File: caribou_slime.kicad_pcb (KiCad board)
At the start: 2 copper layers, 62.7 x 37.6 mm, 37 parts, among them J1 BATT JST, Q1 AO3145, U1 ESP32-C3_SUPERMINI, U2 BMI270, U3 FS312F-G, U4 FS8205A, U5 TP4056, U6 ME6211C33M5G

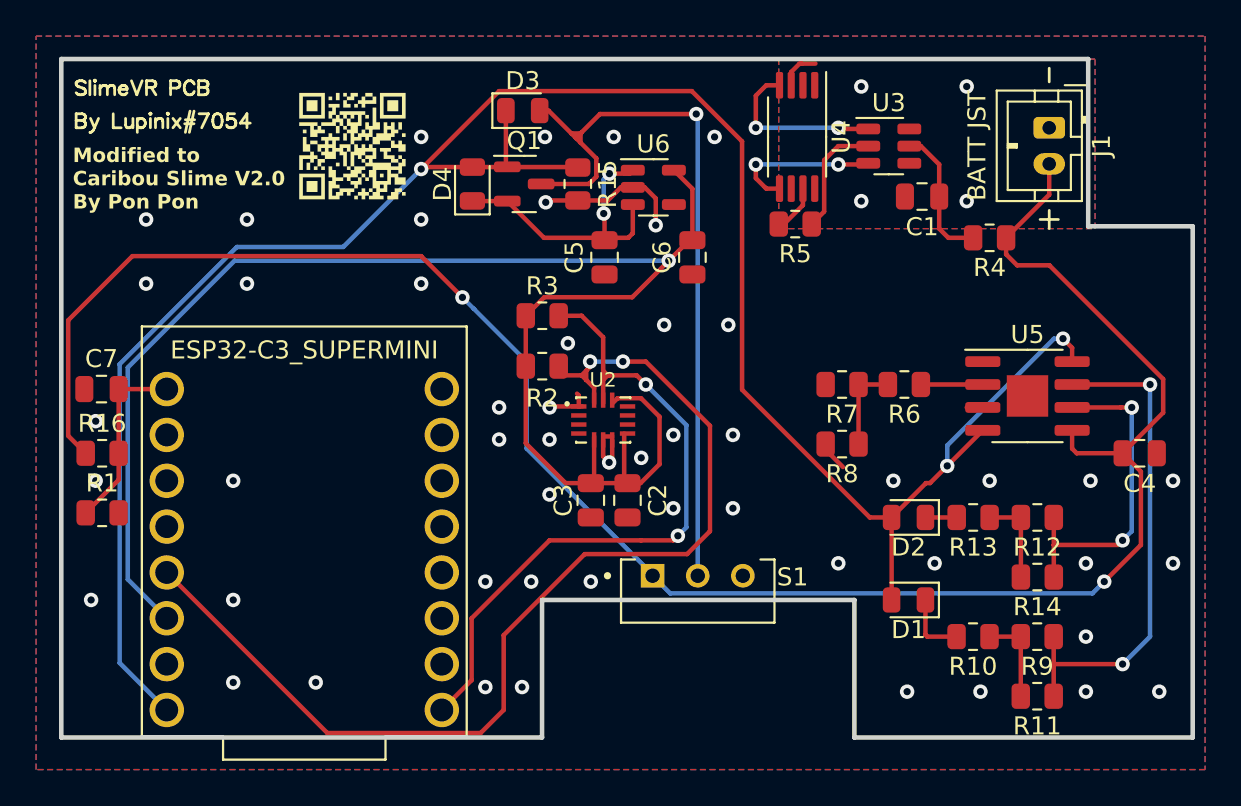
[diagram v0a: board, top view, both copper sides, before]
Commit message: chore(pcb): Improve regulator aesthetics
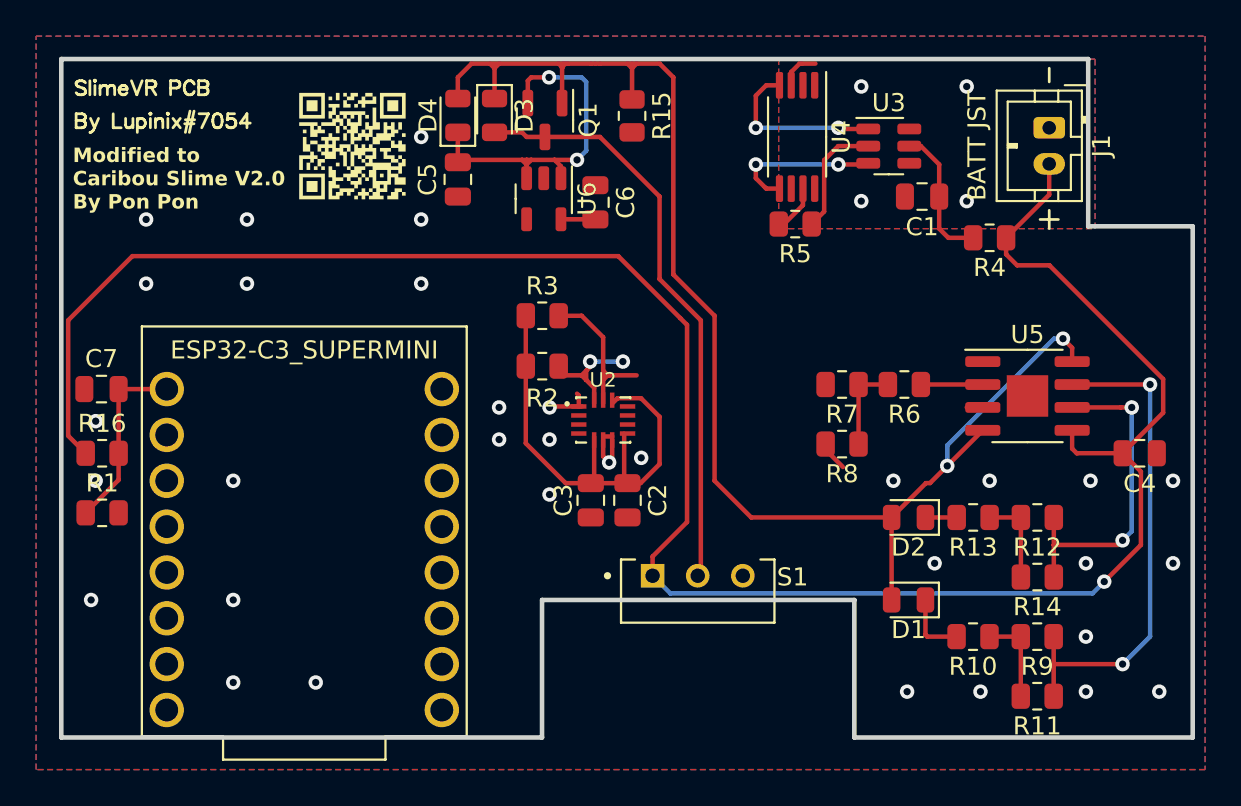
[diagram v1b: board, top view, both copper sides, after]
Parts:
- moved C5 9.20 mm to (47.5, 32.1)
- moved C6 6.18 mm to (55.1, 33.3), turned to -90 degrees
- moved U6 6.10 mm to (52.3, 33.1), turned to -90 degrees
- moved R15 4.82 mm to (57.1, 28.6)
- moved D4 3.88 mm to (47.5, 28.5)
- moved Q1 3.73 mm to (52.3, 28.8), turned to -90 degrees
- moved D3 1.59 mm to (49.5, 28.5), turned to -90 degrees
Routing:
- net +3V3: track 89.6 -> 29.0 mm, vias 1 -> 0
- net SDA: track 59.4 -> 6.40 mm
- net +5V: track 122.1 -> 78.8 mm, vias 3 -> 2
- net SCL: track 38.6 -> 9.28 mm, vias 2 -> 0
- net Net-(D3-A): track 42.4 -> 32.6 mm, vias 1 -> 0
- net GND: track 19.2 -> 11.0 mm, vias 51 -> 33
- net VBAT: track 112.4 -> 120.5 mm, vias 2 -> 1
- net Net-(D4-K): track 16.6 -> 20.4 mm

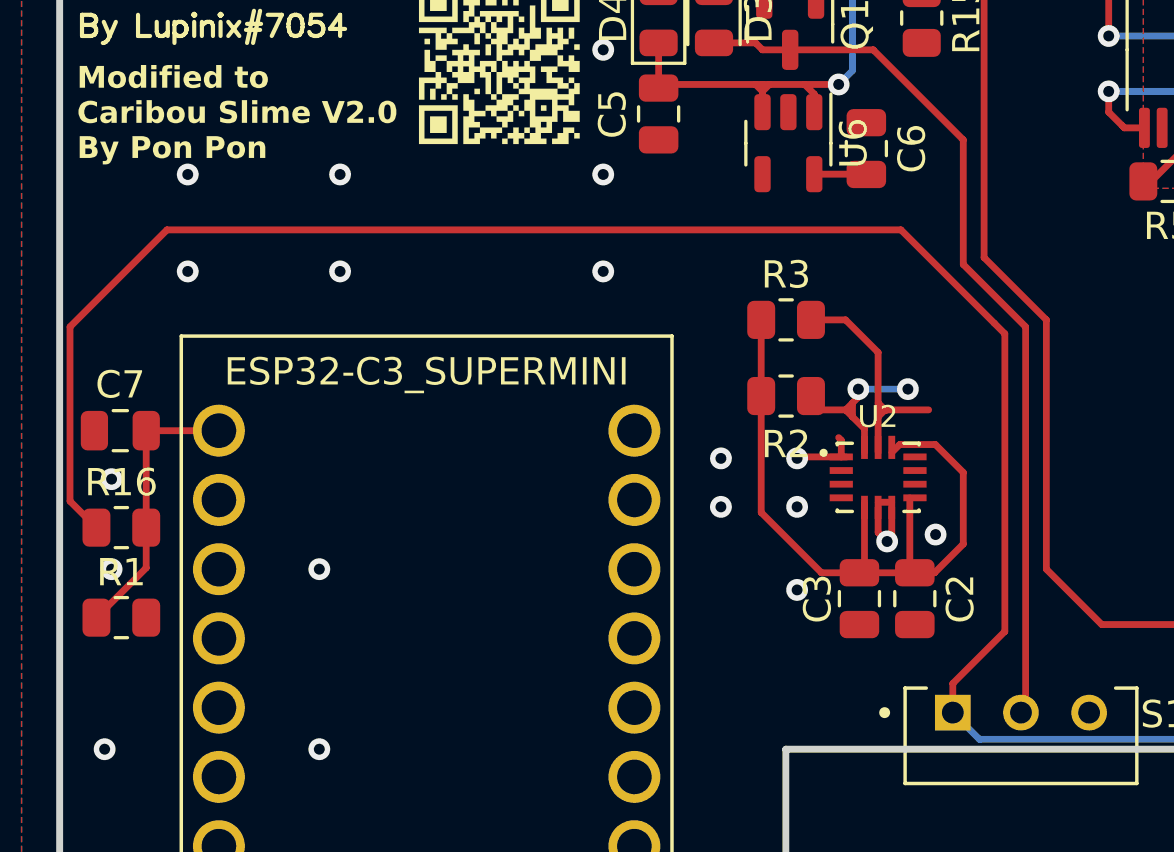
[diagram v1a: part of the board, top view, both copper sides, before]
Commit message: chore(pcb): Improve BMI270 aesthetics
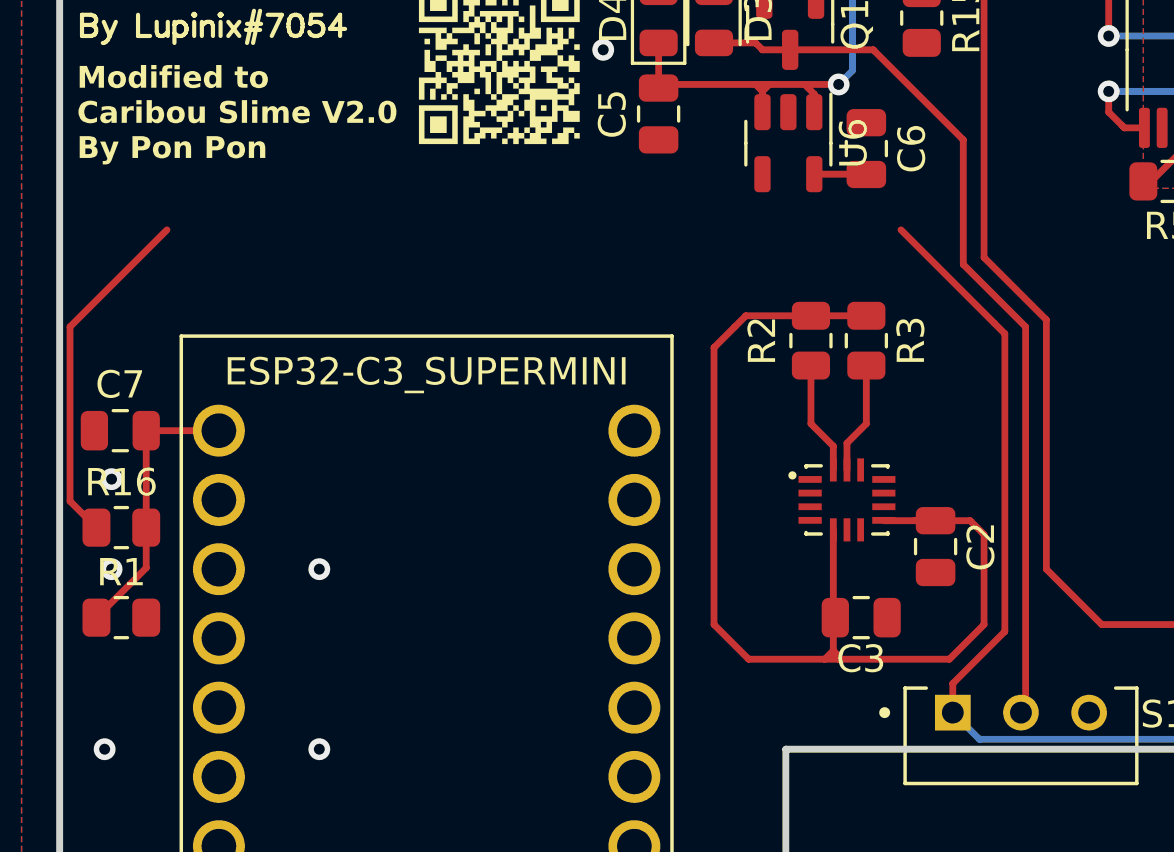
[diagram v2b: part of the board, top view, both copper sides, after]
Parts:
- moved R3 3.04 mm to (55.1, 40.4), turned to -90 degrees
- moved R2 2.23 mm to (53.1, 40.4), turned to -90 degrees
- moved C2 2.06 mm to (57.7, 47.9)
- moved U2 1.41 mm to (54.4, 46.2)
- moved C3 0.70 mm to (54.9, 50.5), turned to 0 degrees
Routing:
- net VBAT: track 120.5 -> 93.5 mm
- net +3V3: track 29.0 -> 41.6 mm
- net GND: track 11.0 -> 5.25 mm, vias 33 -> 20
- net SCL: track 9.28 -> 4.12 mm
- net SDA: track 6.40 -> 4.17 mm, vias 2 -> 0

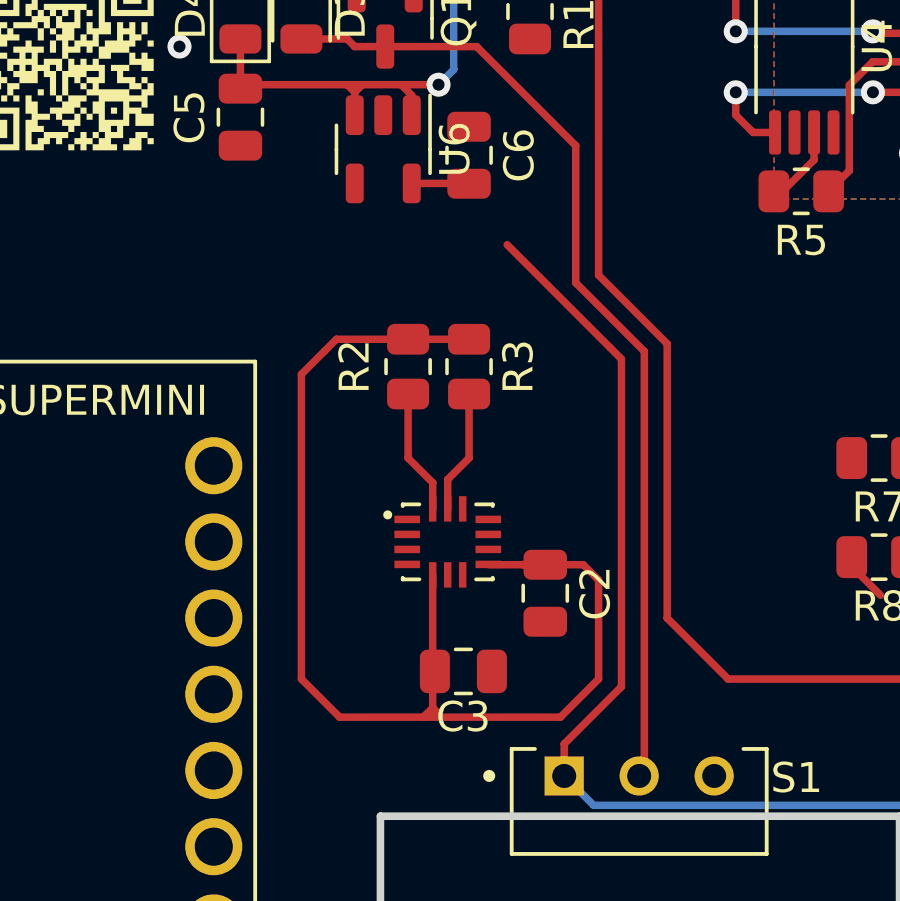
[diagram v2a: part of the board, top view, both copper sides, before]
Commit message: chore(pcb): Improve 270/regulator aesthetics
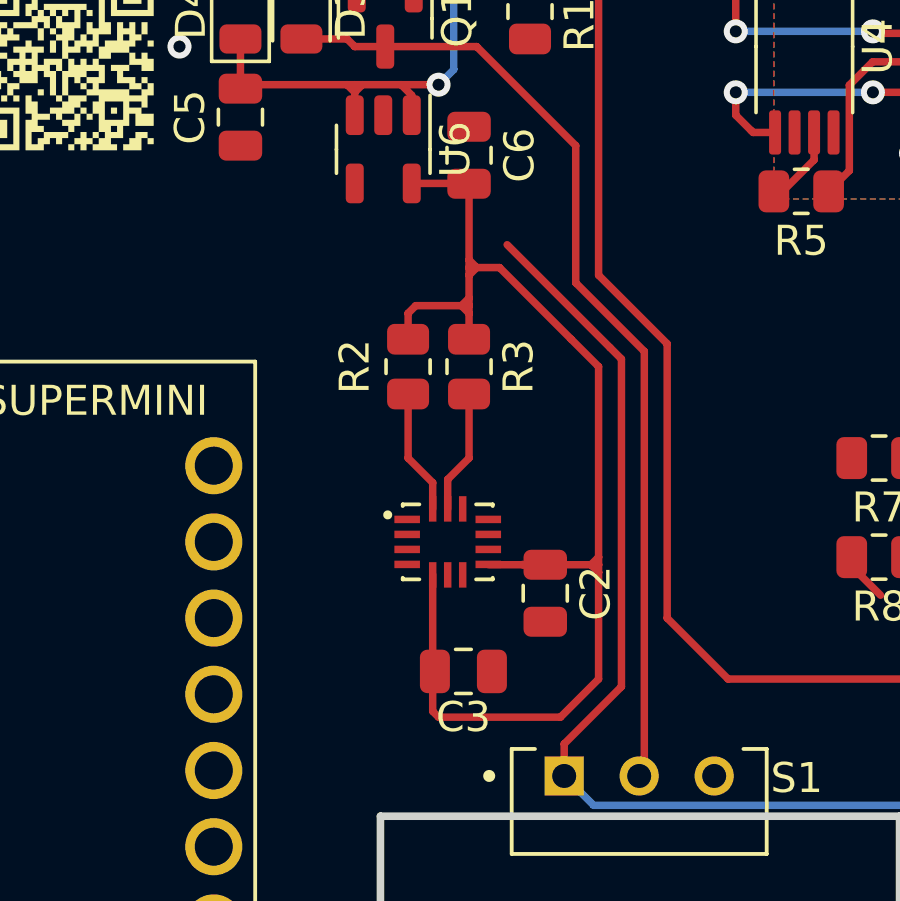
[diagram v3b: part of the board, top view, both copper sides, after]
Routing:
- net +3V3: track 41.6 -> 42.7 mm
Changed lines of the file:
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@@
     (style (thickness 0.15) (arrow_length 1.27) (text_position_mode 0) (extension_height 0.58642) (extension_offset 0.5) keep_text_aligned)
   )
+  (segment (start 59.436 47.244) (end 59.436 46.99) (width 0.25) (layer "F.Cu") (net 1))
+  (segment (start 55.118 34.29) (end 55.118 36.83) (width 0.25) (layer "F.Cu") (net 1))
   (segment (start 55.107 34.279) (end 55.118 34.29) (width 0.25) (layer "F.Cu") (net 1))
-  (segment (start 54.102 52.07) (end 53.594 52.07) (width 0.25) (layer "F.Cu") (net 1))
-  (segment (start 57.658 46.99) (end 58.928 46.99) (width 0.25) (layer "F.Cu") (net 1))
+  (segment (start 55.372 37.084) (end 55.118 37.084) (width 0.25) (layer "F.Cu") (net 1))
+  (segment (start 55.118 38.1) (end 55.118 38.354) (width 0.25) (layer "F.Cu") (net 1))
+  (segment (start 53.34 38.354) (end 54.864 38.354) (width 0.25) (layer "F.Cu") (net 1))
+  (segment (start 59.436 46.736) (end 59.436 40.386) (width 0.25) (layer "F.Cu") (net 1))
+  (segment (start 59.182 46.99) (end 59.436 46.99) (width 0.25) (layer "F.Cu") (net 1))
+  (segment (start 55.118 38.354) (end 55.118 38.608) (width 0.25) (layer "F.Cu") (net 1))
+  (segment (start 58.5235 39.4735) (end 56.134 37.084) (width 0.25) (layer "F.Cu") (net 1))
+  (segment (start 54.102 52.07) (end 58.166 52.07) (width 0.25) (layer "F.Cu") (net 1))
+  (segment (start 59.436 46.99) (end 59.436 46.736) (width 0.25) (layer "F.Cu") (net 1))
+  (segment (start 54.864 38.354) (end 55.118 38.354) (width 0.25) (layer "F.Cu") (net 1))
+  (segment (start 59.436 50.8) (end 59.436 47.244) (width 0.25) (layer "F.Cu") (net 1))
+  (segment (start 58.166 52.07) (end 59.436 50.8) (width 0.25) (layer "F.Cu") (net 1))
   (segment (start 53.208 34.279) (end 55.107 34.279) (width 0.25) (layer "F.Cu") (net 1))
-  (segment (start 53.594 52.07) (end 50.8 52.07) (width 0.25) (layer "F.Cu") (net 1))
   (segment (start 57.658 46.99) (end 55.7705 46.99) (width 0.25) (layer "F.Cu") (net 1))
-  (segment (start 59.436 50.8) (end 58.166 52.07) (width 0.25) (layer "F.Cu") (net 1))
-  (segment (start 53.907 51.757) (end 53.594 52.07) (width 0.25) (layer "F.Cu") (net 1))
+  (segment (start 55.118 37.084) (end 55.118 37.338) (width 0.25) (layer "F.Cu") (net 1))
+  (segment (start 59.182 46.99) (end 59.436 46.736) (width 0.25) (layer "F.Cu") (net 1))
+  (segment (start 53.907 51.875) (end 54.102 52.07) (width 0.25) (layer "F.Cu") (net 1))
+  (segment (start 53.086 38.608) (end 53.34 38.354) (width 0.25) (layer "F.Cu") (net 1))
   (segment (start 56.9135 46.99) (end 56.9015 46.978) (width 0.25) (layer "F.Cu") (net 1))
-  (segment (start 49.53 50.8) (end 50.8 52.07) (width 0.25) (layer "F.Cu") (net 1))
-  (segment (start 53.907 51.757) (end 54.102 51.952) (width 0.25) (layer "F.Cu") (net 1))
-  (segment (start 53.907 47.3275) (end 53.907 51.757) (width 0.25) (layer "F.Cu") (net 1))
-  (segment (start 49.53 40.64) (end 50.292 39.878) (width 0.25) (layer "F.Cu") (net 1))
-  (segment (start 58.928 46.99) (end 59.436 47.498) (width 0.25) (layer "F.Cu") (net 1))
-  (segment (start 54.102 51.952) (end 54.102 52.07) (width 0.25) (layer "F.Cu") (net 1))
-  (segment (start 50.6965 39.4735) (end 50.292 39.878) (width 0.25) (layer "F.Cu") (net 1))
-  (segment (start 49.53 50.8) (end 49.53 40.64) (width 0.25) (layer "F.Cu") (net 1))
-  (segment (start 55.118 39.4735) (end 50.6965 39.4735) (width 0.25) (layer "F.Cu") (net 1))
-  (segment (start 58.166 52.07) (end 54.102 52.07) (width 0.25) (layer "F.Cu") (net 1))
-  (segment (start 59.436 47.498) (end 59.436 50.8) (width 0.25) (layer "F.Cu") (net 1))
+  (segment (start 53.086 39.4735) (end 53.086 38.608) (width 0.25) (layer "F.Cu") (net 1))
+  (segment (start 55.372 37.084) (end 55.118 37.338) (width 0.25) (layer "F.Cu") (net 1))
+  (segment (start 56.134 37.084) (end 55.372 37.084) (width 0.25) (layer "F.Cu") (net 1))
+  (segment (start 55.118 37.338) (end 55.118 38.1) (width 0.25) (layer "F.Cu") (net 1))
+  (segment (start 54.864 38.354) (end 55.118 38.608) (width 0.25) (layer "F.Cu") (net 1))
+  (segment (start 55.118 38.608) (end 55.118 39.4735) (width 0.25) (layer "F.Cu") (net 1))
+  (segment (start 59.436 40.386) (end 58.5235 39.4735) (width 0.25) (layer "F.Cu") (net 1))
+  (segment (start 54.864 38.354) (end 55.118 38.1) (width 0.25) (layer "F.Cu") (net 1))
+  (segment (start 55.372 37.084) (end 55.118 36.83) (width 0.25) (layer "F.Cu") (net 1))
+  (segment (start 55.118 36.83) (end 55.118 37.084) (width 0.25) (layer "F.Cu") (net 1))
+  (segment (start 53.907 47.3275) (end 53.907 51.875) (width 0.25) (layer "F.Cu") (net 1))
+  (segment (start 59.182 46.99) (end 59.436 47.244) (width 0.25) (layer "F.Cu") (net 1))
+  (segment (start 57.658 46.99) (end 59.182 46.99) (width 0.25) (layer "F.Cu") (net 1))
   (segment (start 53.274 27.843) (end 53.274 25.908) (width 0.25) (layer "F.Cu") (net 9))
   (segment (start 49.276 25.654) (end 49.784 25.654) (width 0.25) (layer "F.Cu") (net 9))
@@
     (polygon
       (pts
-        (xy 32.512 39.37)
-        (xy 45.466 39.37)
-        (xy 45.466 44.704)
-        (xy 32.512 44.704)
+        (xy 33.528 40.386)
+        (xy 44.704 40.386)
+        (xy 44.704 44.704)
+        (xy 33.528 44.704)
       )
     )
